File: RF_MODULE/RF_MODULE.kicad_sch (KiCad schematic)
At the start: 65 parts, among them J1 Conn_01x04, J2 POWER IN, J3 Conn_Coaxial, Q1 2SC1740, Q2 2SC461, SW1 PW_SW, SW2 CH-SW, U1 HA17805

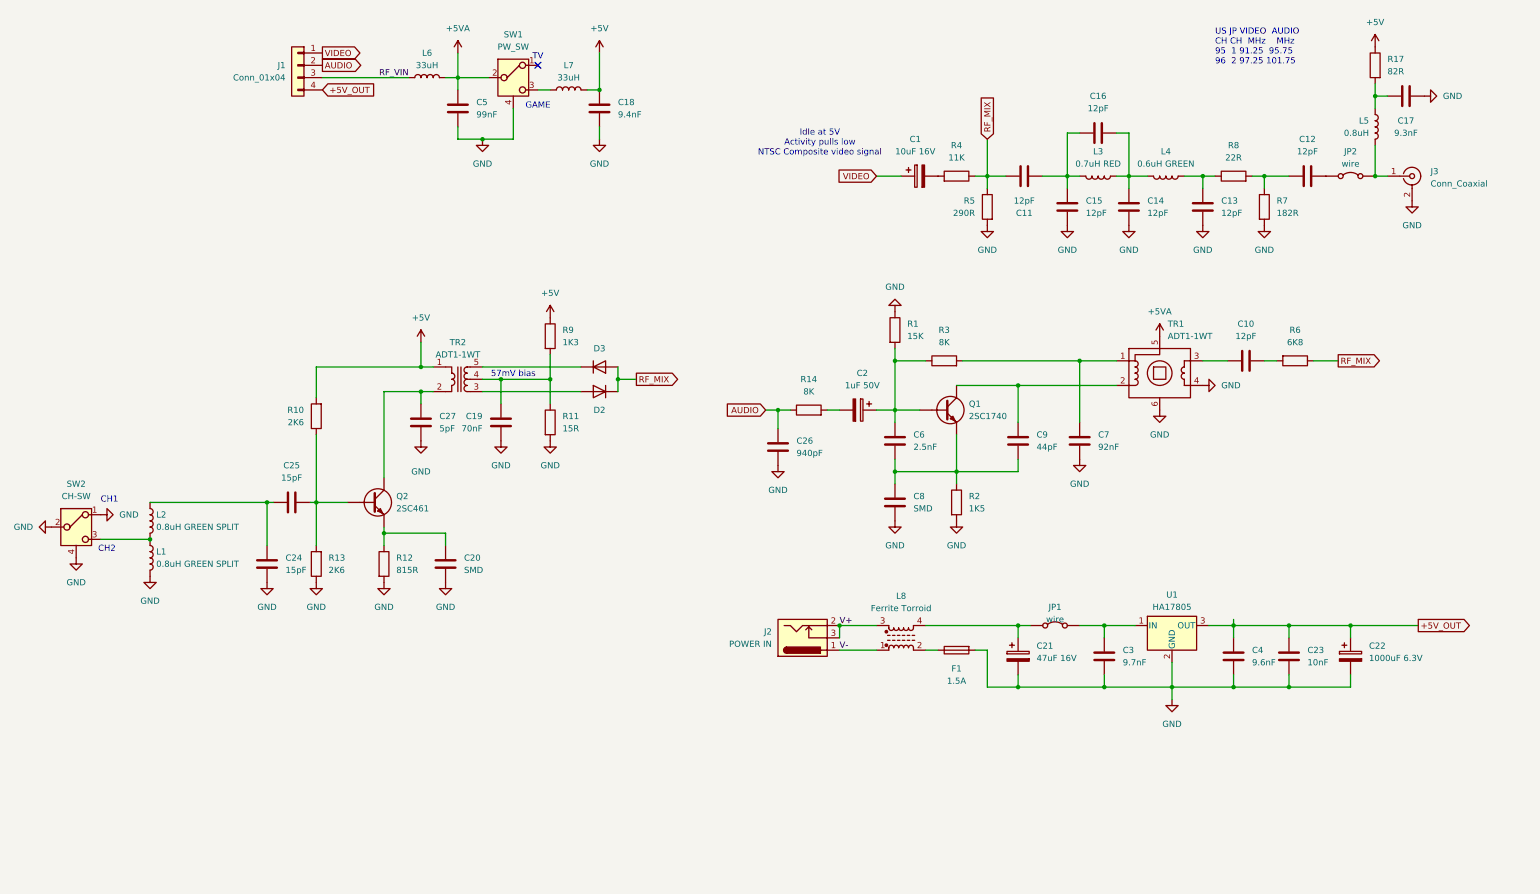
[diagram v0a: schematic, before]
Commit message: clean up RF modulator schematic and PCB
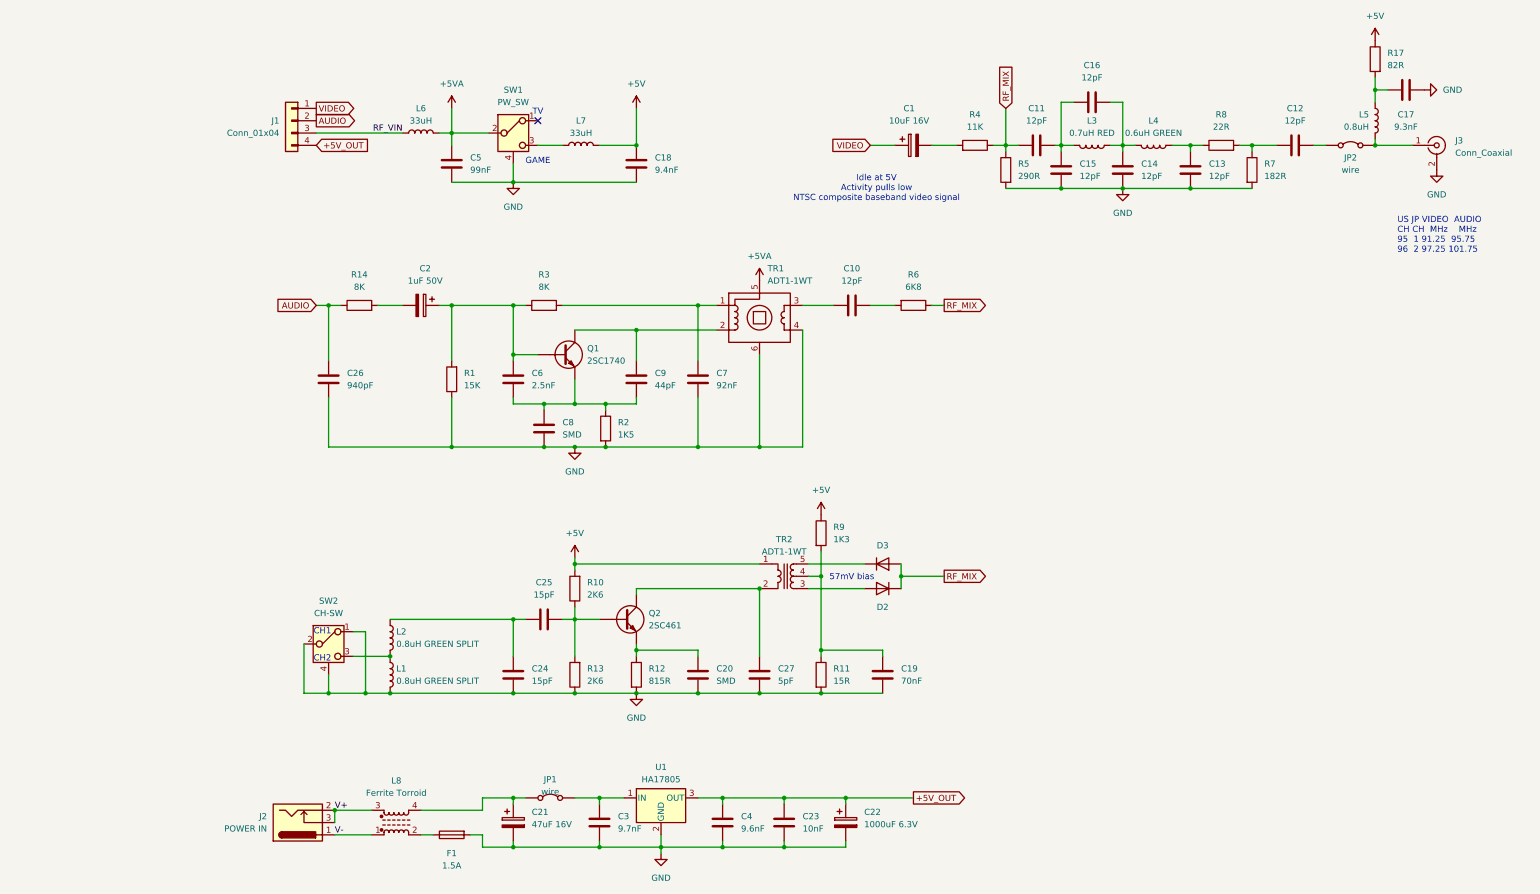
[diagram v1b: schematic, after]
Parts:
- D2, D3: footprint Diode_THT:D_T-1_P5.08mm_Horizontal -> nintendo:D_5p
- R17: footprint Resistor_THT:R_Axial_DIN0207_L6.3mm_D2.5mm_P10.16mm_Horizontal -> nintendo:R_10p
- R6: footprint Resistor_THT:R_Axial_DIN0204_L3.6mm_D1.6mm_P5.08mm_Horizontal -> nintendo:R_5p
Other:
- note added: "Idle at 5V Activity pulls low NTSC composite baseband video signal"
- note removed: "Idle at 5V Activity pulls low NTSC Composite video signal"
- moved on the sheet: C1, C10, C11, C12, C13, C14, C15, C16, C17, C18, C19, C2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
